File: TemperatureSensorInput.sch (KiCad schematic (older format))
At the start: 3 parts, among them J8 TEMP 1

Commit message: preliminary placement done
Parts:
- J8: footprint Connector_JST:JST_GH_SM02B-GHS-TB_1x02-1MP_P1.25mm_Horizontal -> Connector_JST:JST_GH_BM02B-GHS-TBT_1x02-1MP_P1.25mm_Vertical
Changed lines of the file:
@@
 F 0 "J8" H 5680 3942 50  0000 L CNN
 F 1 "TEMP 1" H 5680 3851 50  0000 L CNN
-F 2 "Connector_JST:JST_GH_SM02B-GHS-TB_1x02-1MP_P1.25mm_Horizontal" H 5600 3950 50  0001 C CNN
+F 2 "Connector_JST:JST_GH_BM02B-GHS-TBT_1x02-1MP_P1.25mm_Vertical" H 5600 3950 50  0001 C CNN
 F 3 "~" H 5600 3950 50  0001 C CNN
 	1    5600 3950
@@
 AR Path="/63DF022A/633F40E9" Ref="#PWR0162"  Part="1"
 AR Path="/63E36C88/633F40E9" Ref="#PWR0164"  Part="1"
-F 0 "#PWR0164" H 5825 3425 50  0001 C CNN
+F 0 "#PWR0112" H 5825 3425 50  0001 C CNN
 F 1 "+3V3" H 5825 3725 50  0000 C CNN
 F 2 "" H 5825 3575 50  0001 C CNN
@@
 AR Path="/63DF022A/633F40F3" Ref="#PWR0163"  Part="1"
 AR Path="/63E36C88/633F40F3" Ref="#PWR0165"  Part="1"
-F 0 "#PWR0165" H 5825 3875 50  0001 C CNN
+F 0 "#PWR0113" H 5825 3875 50  0001 C CNN
 F 1 "GND" H 5825 3975 50  0000 C CNN
 F 2 "" H 5825 4125 50  0001 C CNN

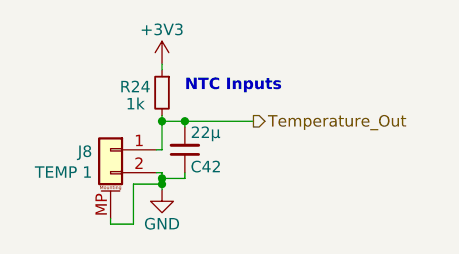
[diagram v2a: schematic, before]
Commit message: moved 7V4 buck to separate board
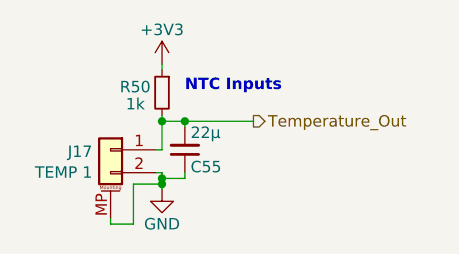
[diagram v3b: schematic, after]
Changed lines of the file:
@@
 AR Path="/63DF022A/633F40CA" Ref="R49"  Part="1"
 AR Path="/63E36C88/633F40CA" Ref="R50"  Part="1"
-F 0 "R24" H 5875 3725 50  0000 L CNN
+F 0 "R50" H 5875 3725 50  0000 L CNN
 F 1 "1k" H 5900 3650 50  0000 L CNN
 F 2 "Resistor_SMD:R_0603_1608Metric" H 5825 3700 50  0001 C CNN
@@
 AR Path="/63DF022A/633F40D2" Ref="J16"  Part="1"
 AR Path="/63E36C88/633F40D2" Ref="J17"  Part="1"
-F 0 "J8" H 5680 3942 50  0000 L CNN
+F 0 "J17" H 5680 3942 50  0000 L CNN
 F 1 "TEMP 1" H 5680 3851 50  0000 L CNN
 F 2 "Connector_JST:JST_GH_BM02B-GHS-TBT_1x02-1MP_P1.25mm_Vertical" H 5600 3950 50  0001 C CNN
@@
 AR Path="/63DF022A/633F40D8" Ref="C54"  Part="1"
 AR Path="/63E36C88/633F40D8" Ref="C55"  Part="1"
-F 0 "C42" H 5950 4025 50  0000 L CNN
+F 0 "C55" H 5950 4025 50  0000 L CNN
 F 1 "22µ" H 5950 3875 50  0000 L CNN
 F 2 "Capacitor_SMD:C_0603_1608Metric" H 5925 3950 50  0001 C CNN

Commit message: many small changes, before removing servo buck converter
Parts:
- added R71: 9k1, Resistor_SMD:R_0603_1608Metric, symbol Device:R_Small
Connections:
- net Temperature_Out: now also R71.1; no longer C42.2, J8.1 (Pin_1), R24.2
- new net: C42.2, J8.1 (Pin_1), R24.2, R71.2
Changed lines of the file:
@@
 AR Path="/63DF022A/633F40CA" Ref="R49"  Part="1"
 AR Path="/63E36C88/633F40CA" Ref="R50"  Part="1"
-F 0 "R50" H 5875 3725 50  0000 L CNN
+F 0 "R24" H 5875 3725 50  0000 L CNN
 F 1 "1k" H 5900 3650 50  0000 L CNN
 F 2 "Resistor_SMD:R_0603_1608Metric" H 5825 3700 50  0001 C CNN
@@
 	-1   0    0    -1
 $EndComp
-Text Notes 5925 3700 0    50   ~ 10
+Text Notes 6025 3550 0    50   ~ 10
 NTC Inputs
 $Comp
@@
 AR Path="/63DF022A/633F40D2" Ref="J16"  Part="1"
 AR Path="/63E36C88/633F40D2" Ref="J17"  Part="1"
-F 0 "J17" H 5680 3942 50  0000 L CNN
+F 0 "J8" H 5680 3942 50  0000 L CNN
 F 1 "TEMP 1" H 5680 3851 50  0000 L CNN
 F 2 "Connector_JST:JST_GH_BM02B-GHS-TBT_1x02-1MP_P1.25mm_Vertical" H 5600 3950 50  0001 C CNN
@@
 AR Path="/63DF022A/633F40D8" Ref="C54"  Part="1"
 AR Path="/63E36C88/633F40D8" Ref="C55"  Part="1"
-F 0 "C55" H 5950 4025 50  0000 L CNN
-F 1 "22µ" H 5950 3875 50  0000 L CNN
+F 0 "C42" H 6000 3950 50  0000 L CNN
+F 1 "22µ" H 5950 4025 50  0000 L CNN
 F 2 "Capacitor_SMD:C_0603_1608Metric" H 5925 3950 50  0001 C CNN
 F 3 "" H 5925 3950 50  0001 C CNN
@@
 AR Path="/63DF022A/633F40E9" Ref="#PWR0162"  Part="1"
 AR Path="/63E36C88/633F40E9" Ref="#PWR0164"  Part="1"
-F 0 "#PWR0164" H 5825 3425 50  0001 C CNN
+F 0 "#PWR0112" H 5825 3425 50  0001 C CNN
 F 1 "+3V3" H 5825 3725 50  0000 C CNN
 F 2 "" H 5825 3575 50  0001 C CNN
@@
 Wire Wire Line
 	5825 3575 5825 3600
-Wire Wire Line
-	6225 3825 5925 3825
-Connection ~ 5925 3825
 Wire Wire Line
 	5825 4125 5825 4100
@@
 AR Path="/63DF022A/633F40F3" Ref="#PWR0163"  Part="1"
 AR Path="/63E36C88/633F40F3" Ref="#PWR0165"  Part="1"
-F 0 "#PWR0165" H 5825 3875 50  0001 C CNN
+F 0 "#PWR0113" H 5825 3875 50  0001 C CNN
 F 1 "GND" H 5825 3975 50  0000 C CNN
 F 2 "" H 5825 4125 50  0001 C CNN
@@
 Text HLabel 6225 3825 2    50   Output ~ 0
 Temperature_Out
+$Comp
+L Device:R_Small R?
+U 1 1 61BD0A9D
+P 6075 3825
+AR Path="/61BD0A9D" Ref="R?"  Part="1"
+AR Path="/63324C42/61BD0A9D" Ref="R71"  Part="1"
+AR Path="/63DF022A/61BD0A9D" Ref="R72"  Part="1"
+AR Path="/63E36C88/61BD0A9D" Ref="R73"  Part="1"
+F 0 "R71" V 6150 3675 50  0000 L CNN
+F 1 "9k1" V 6150 3850 50  0000 L CNN
+F 2 "Resistor_SMD:R_0603_1608Metric" H 6075 3825 50  0001 C CNN
+F 3 "~" H 6075 3825 50  0001 C CNN
+	1    6075 3825
+	0    1    -1   0
+$EndComp
+Wire Wire Line
+	5975 3825 5925 3825
+Connection ~ 5925 3825
+Wire Wire Line
+	6175 3825 6225 3825
 $EndSCHEMATC

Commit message: placement almost done
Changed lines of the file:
@@
 $Descr A4 11693 8268
 encoding utf-8
-Sheet 3 17
+Sheet 3 18
 Title ""
 Date ""
@@
 AR Path="/63DF022A/633F40CA" Ref="R49"  Part="1"
 AR Path="/63E36C88/633F40CA" Ref="R50"  Part="1"
-F 0 "R24" H 5875 3725 50  0000 L CNN
+F 0 "R50" H 5875 3725 50  0000 L CNN
 F 1 "1k" H 5900 3650 50  0000 L CNN
 F 2 "Resistor_SMD:R_0603_1608Metric" H 5825 3700 50  0001 C CNN
@@
 AR Path="/63DF022A/633F40D2" Ref="J16"  Part="1"
 AR Path="/63E36C88/633F40D2" Ref="J17"  Part="1"
-F 0 "J8" H 5680 3942 50  0000 L CNN
+F 0 "J17" H 5680 3942 50  0000 L CNN
 F 1 "TEMP 1" H 5680 3851 50  0000 L CNN
 F 2 "Connector_JST:JST_GH_BM02B-GHS-TBT_1x02-1MP_P1.25mm_Vertical" H 5600 3950 50  0001 C CNN
@@
 AR Path="/63DF022A/633F40D8" Ref="C54"  Part="1"
 AR Path="/63E36C88/633F40D8" Ref="C55"  Part="1"
-F 0 "C42" H 6000 3950 50  0000 L CNN
+F 0 "C55" H 6000 3950 50  0000 L CNN
 F 1 "22µ" H 5950 4025 50  0000 L CNN
 F 2 "Capacitor_SMD:C_0603_1608Metric" H 5925 3950 50  0001 C CNN
@@
 AR Path="/63DF022A/633F40E9" Ref="#PWR0162"  Part="1"
 AR Path="/63E36C88/633F40E9" Ref="#PWR0164"  Part="1"
-F 0 "#PWR0112" H 5825 3425 50  0001 C CNN
+F 0 "#PWR0164" H 5825 3425 50  0001 C CNN
 F 1 "+3V3" H 5825 3725 50  0000 C CNN
 F 2 "" H 5825 3575 50  0001 C CNN
@@
 AR Path="/63DF022A/633F40F3" Ref="#PWR0163"  Part="1"
 AR Path="/63E36C88/633F40F3" Ref="#PWR0165"  Part="1"
-F 0 "#PWR0113" H 5825 3875 50  0001 C CNN
+F 0 "#PWR0165" H 5825 3875 50  0001 C CNN
 F 1 "GND" H 5825 3975 50  0000 C CNN
 F 2 "" H 5825 4125 50  0001 C CNN
@@
 AR Path="/63DF022A/61BD0A9D" Ref="R72"  Part="1"
 AR Path="/63E36C88/61BD0A9D" Ref="R73"  Part="1"
-F 0 "R71" V 6150 3675 50  0000 L CNN
+F 0 "R73" V 6150 3675 50  0000 L CNN
 F 1 "9k1" V 6150 3850 50  0000 L CNN
 F 2 "Resistor_SMD:R_0603_1608Metric" H 6075 3825 50  0001 C CNN

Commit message: fixed net names
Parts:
- J8: value TEMP 1 -> TEMP
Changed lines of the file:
@@
 $Descr A4 11693 8268
 encoding utf-8
-Sheet 3 18
+Sheet 12 18
 Title ""
 Date ""
@@
 AR Path="/63E36C88/633F40D2" Ref="J17"  Part="1"
 F 0 "J17" H 5680 3942 50  0000 L CNN
-F 1 "TEMP 1" H 5680 3851 50  0000 L CNN
+F 1 "TEMP" H 5680 3851 50  0000 L CNN
 F 2 "Connector_JST:JST_GH_BM02B-GHS-TBT_1x02-1MP_P1.25mm_Vertical" H 5600 3950 50  0001 C CNN
 F 3 "~" H 5600 3950 50  0001 C CNN

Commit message: routing started
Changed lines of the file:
@@
 $Descr A4 11693 8268
 encoding utf-8
-Sheet 12 18
+Sheet 11 18
 Title ""
 Date ""
@@
 AR Path="/63DF022A/633F40CA" Ref="R49"  Part="1"
 AR Path="/63E36C88/633F40CA" Ref="R50"  Part="1"
-F 0 "R50" H 5875 3725 50  0000 L CNN
+F 0 "R49" H 5875 3725 50  0000 L CNN
 F 1 "1k" H 5900 3650 50  0000 L CNN
 F 2 "Resistor_SMD:R_0603_1608Metric" H 5825 3700 50  0001 C CNN
@@
 AR Path="/63DF022A/633F40D2" Ref="J16"  Part="1"
 AR Path="/63E36C88/633F40D2" Ref="J17"  Part="1"
-F 0 "J17" H 5680 3942 50  0000 L CNN
+F 0 "J16" H 5680 3942 50  0000 L CNN
 F 1 "TEMP" H 5680 3851 50  0000 L CNN
 F 2 "Connector_JST:JST_GH_BM02B-GHS-TBT_1x02-1MP_P1.25mm_Vertical" H 5600 3950 50  0001 C CNN
@@
 AR Path="/63DF022A/633F40D8" Ref="C54"  Part="1"
 AR Path="/63E36C88/633F40D8" Ref="C55"  Part="1"
-F 0 "C55" H 6000 3950 50  0000 L CNN
+F 0 "C54" H 6000 3950 50  0000 L CNN
 F 1 "22µ" H 5950 4025 50  0000 L CNN
 F 2 "Capacitor_SMD:C_0603_1608Metric" H 5925 3950 50  0001 C CNN
@@
 AR Path="/63DF022A/61BD0A9D" Ref="R72"  Part="1"
 AR Path="/63E36C88/61BD0A9D" Ref="R73"  Part="1"
-F 0 "R73" V 6150 3675 50  0000 L CNN
+F 0 "R72" V 6150 3675 50  0000 L CNN
 F 1 "9k1" V 6150 3850 50  0000 L CNN
 F 2 "Resistor_SMD:R_0603_1608Metric" H 6075 3825 50  0001 C CNN

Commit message: routing done, drc clean (3 errors to be ignored)
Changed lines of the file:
@@
 AR Path="/63DF022A/633F40CA" Ref="R49"  Part="1"
 AR Path="/63E36C88/633F40CA" Ref="R50"  Part="1"
-F 0 "R49" H 5875 3725 50  0000 L CNN
+F 0 "R50" H 5875 3725 50  0000 L CNN
 F 1 "1k" H 5900 3650 50  0000 L CNN
 F 2 "Resistor_SMD:R_0603_1608Metric" H 5825 3700 50  0001 C CNN
@@
 AR Path="/63DF022A/633F40D2" Ref="J16"  Part="1"
 AR Path="/63E36C88/633F40D2" Ref="J17"  Part="1"
-F 0 "J16" H 5680 3942 50  0000 L CNN
+F 0 "J17" H 5680 3942 50  0000 L CNN
 F 1 "TEMP" H 5680 3851 50  0000 L CNN
 F 2 "Connector_JST:JST_GH_BM02B-GHS-TBT_1x02-1MP_P1.25mm_Vertical" H 5600 3950 50  0001 C CNN
@@
 AR Path="/63DF022A/633F40D8" Ref="C54"  Part="1"
 AR Path="/63E36C88/633F40D8" Ref="C55"  Part="1"
-F 0 "C54" H 6000 3950 50  0000 L CNN
+F 0 "C55" H 6000 3950 50  0000 L CNN
 F 1 "22µ" H 5950 4025 50  0000 L CNN
 F 2 "Capacitor_SMD:C_0603_1608Metric" H 5925 3950 50  0001 C CNN
@@
 AR Path="/63DF022A/61BD0A9D" Ref="R72"  Part="1"
 AR Path="/63E36C88/61BD0A9D" Ref="R73"  Part="1"
-F 0 "R72" V 6150 3675 50  0000 L CNN
+F 0 "R73" V 6150 3675 50  0000 L CNN
 F 1 "9k1" V 6150 3850 50  0000 L CNN
 F 2 "Resistor_SMD:R_0603_1608Metric" H 6075 3825 50  0001 C CNN
